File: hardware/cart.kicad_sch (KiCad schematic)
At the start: 10 parts, among them J4 debug-snoop, P1 edge connector, U1 74LVC138A, U2 MCP1827S-3302E/EB

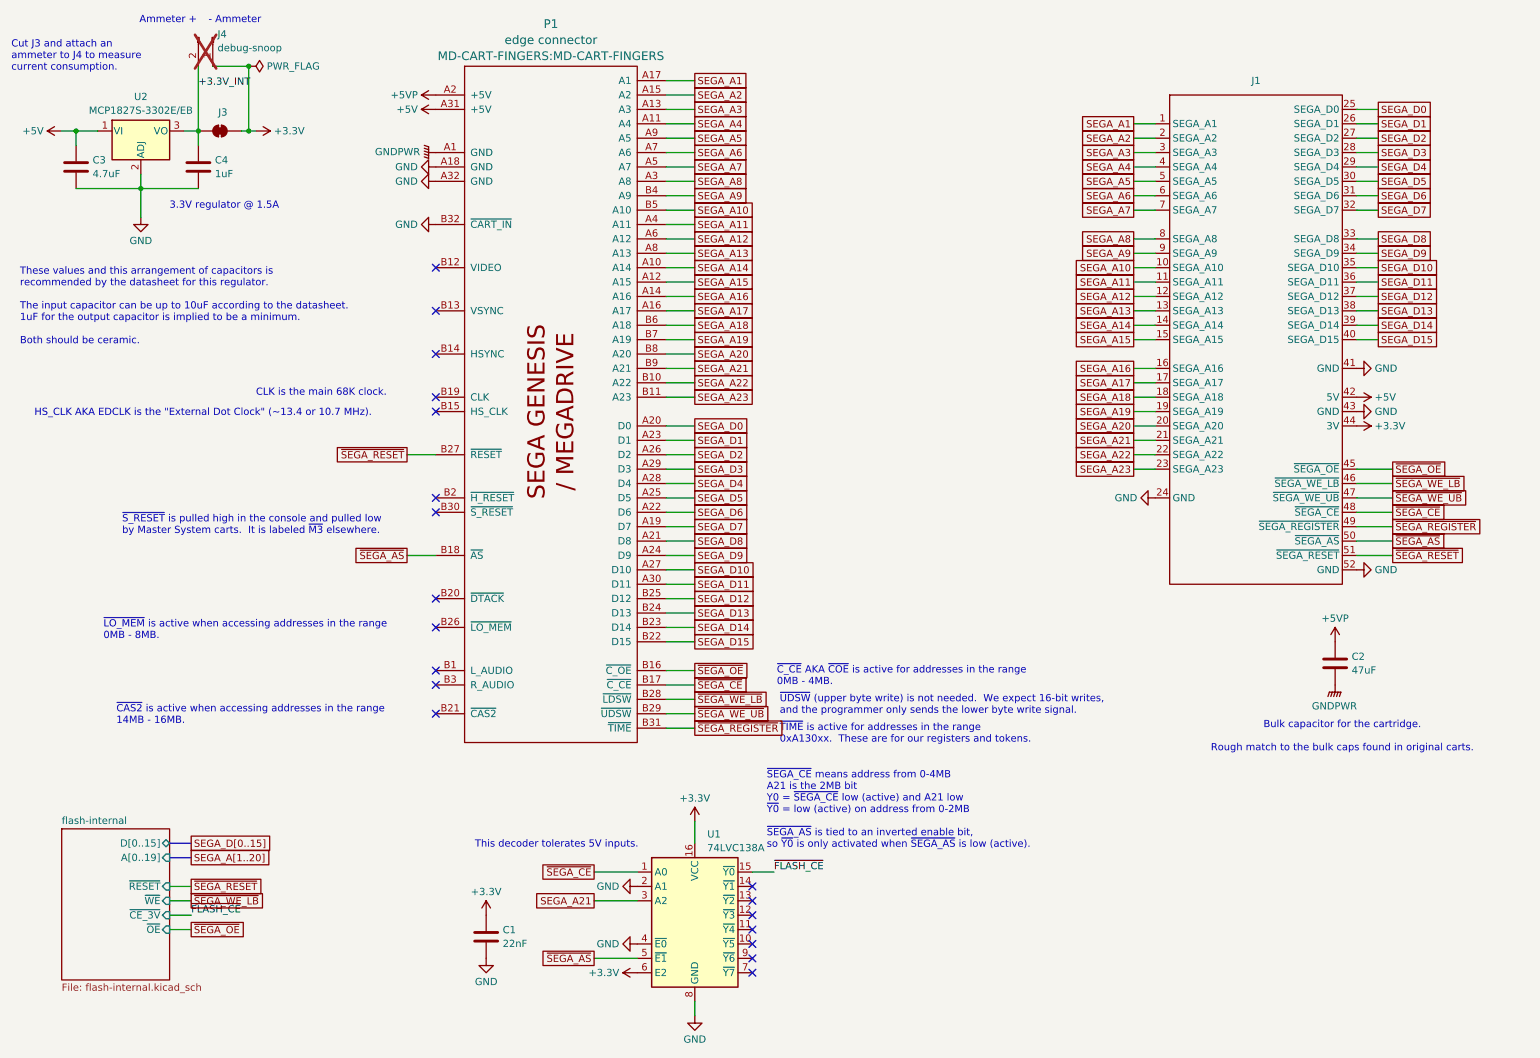
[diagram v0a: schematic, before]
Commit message: Move cart design into shareable subsheet
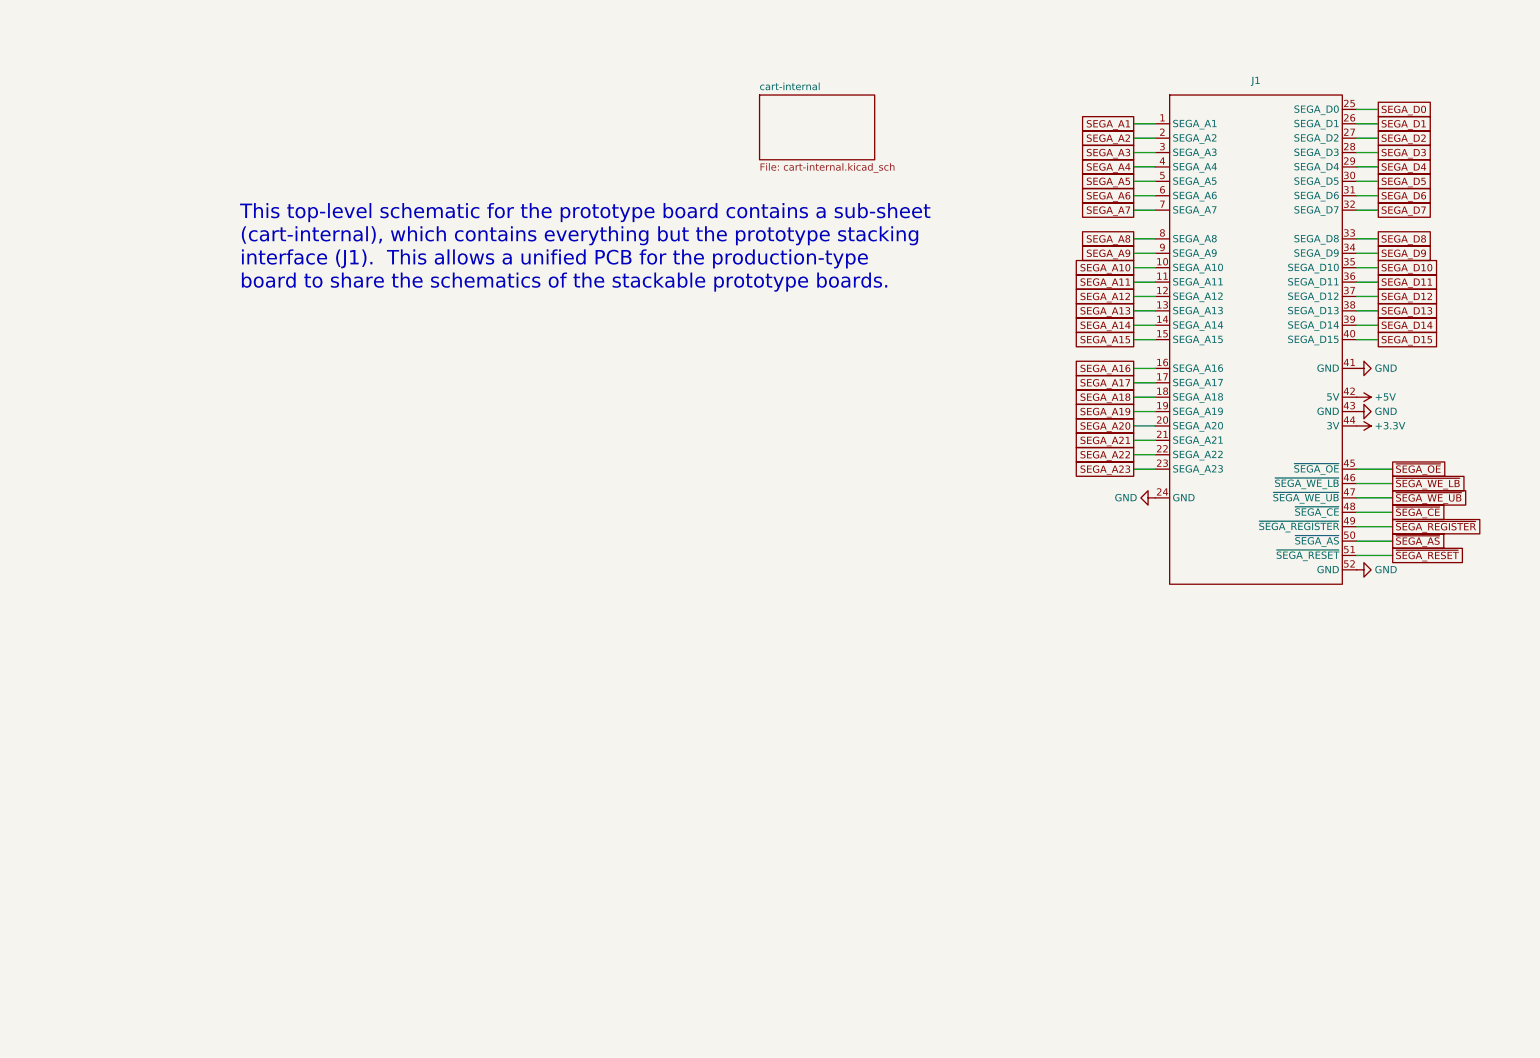
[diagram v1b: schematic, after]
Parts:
- removed C1: 22nF, Capacitor_SMD:C_0603_1608Metric, symbol Device:C
- removed C2: 47uF, Capacitor_SMD:C_1206_3216Metric, symbol Device:C
- removed C3: 4.7uF, Capacitor_SMD:C_0603_1608Metric, symbol Device:C
- removed C4: 1uF, Capacitor_SMD:C_0603_1608Metric, symbol Device:C
- removed J3: ~, Jumper:SolderJumper-2_P1.3mm_Bridged_Pad1.0x1.5mm, symbol Jumper:SolderJumper_2_Bridged
- removed J4: debug-snoop, Connector_PinHeader_2.54mm:PinHeader_1x02_P2.54mm_Horizontal, symbol Connector:Conn_01x02_Pin
- removed P1: edge connector, MD-CART-FINGERS:MD-CART-FINGERS, symbol MD-CART-FINGERS:MD-CART-FINGERS
- removed U1: 74LVC138A, Package_SO:TSSOP-16_4.4x5mm_P0.65mm, symbol 74xx:74HC138
- removed U2: MCP1827S-3302E/EB, Package_TO_SOT_SMD:TO-252-3_TabPin2, symbol Regulator_Linear:LM317_TO39
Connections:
- no-connect marks 19 -> 0
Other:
- removed sheet flash-internal
- added sheet cart-internal (cart-internal.kicad_sch)
- note added: "This top-level schematic for the prototype board contains a sub-sheet (cart-internal), which contains everything but the prototype stacking interface (J1). This allows a unified PCB for the production-type board to share the schematics of the stackable prototype boards."
- note removed: "- Ammeter"
- note removed: "3.3V regulator @ 1.5A"
- note removed: "Ammeter +"
- note removed: "Bulk capacitor for the cartridge. Rough match to the bulk caps found in original carts."
- note removed: "CLK is the main 68K clock."
- note removed: "Cut J3 and attach an ammeter to J4 to measure current consumption."
- note removed: "HS_CLK AKA EDCLK is the "External Dot Clock" (~13.4 or 10.7 MHz)."
- note removed: "These values and this arrangement of capacitors is recommended by the datasheet for this regulator. The input capacitor can be up to 10uF according to the datasheet. 1uF for the output capacitor is implied to be a minimum. Both should be ceramic."
- note removed: "This decoder tolerates 5V inputs."
- note removed: "~{CAS2} is active when accessing addresses in the range 14MB - 16MB."
- note removed: "~{C_CE} AKA ~{COE} is active for addresses in the range 0MB - 4MB."
- note removed: "~{LO_MEM} is active when accessing addresses in the range 0MB - 8MB."
- note removed: "~{SEGA_CE} means address from 0-4MB A21 is the 2MB bit Y0 = ~{SEGA_CE} low (active) and A21 low ~{Y0} = low (active) on address from 0-2MB ~{SEGA_AS} is tied to an inverted enable bit, so ~{Y0} is only activated when ~{SEGA_AS} is low (active)."
- note removed: "~{S_RESET} is pulled high in the console and pulled low by Master System carts. It is labeled ~{M3} elsewhere."
- note removed: "~{TIME} is active for addresses in the range 0xA130xx. These are for our registers and tokens."
- note removed: "~{UDSW} (upper byte write) is not needed. We expect 16-bit writes, and the programmer only sends the lower byte write signal."
